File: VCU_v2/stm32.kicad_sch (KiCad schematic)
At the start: 1 part, among them J1 Conn_01x04

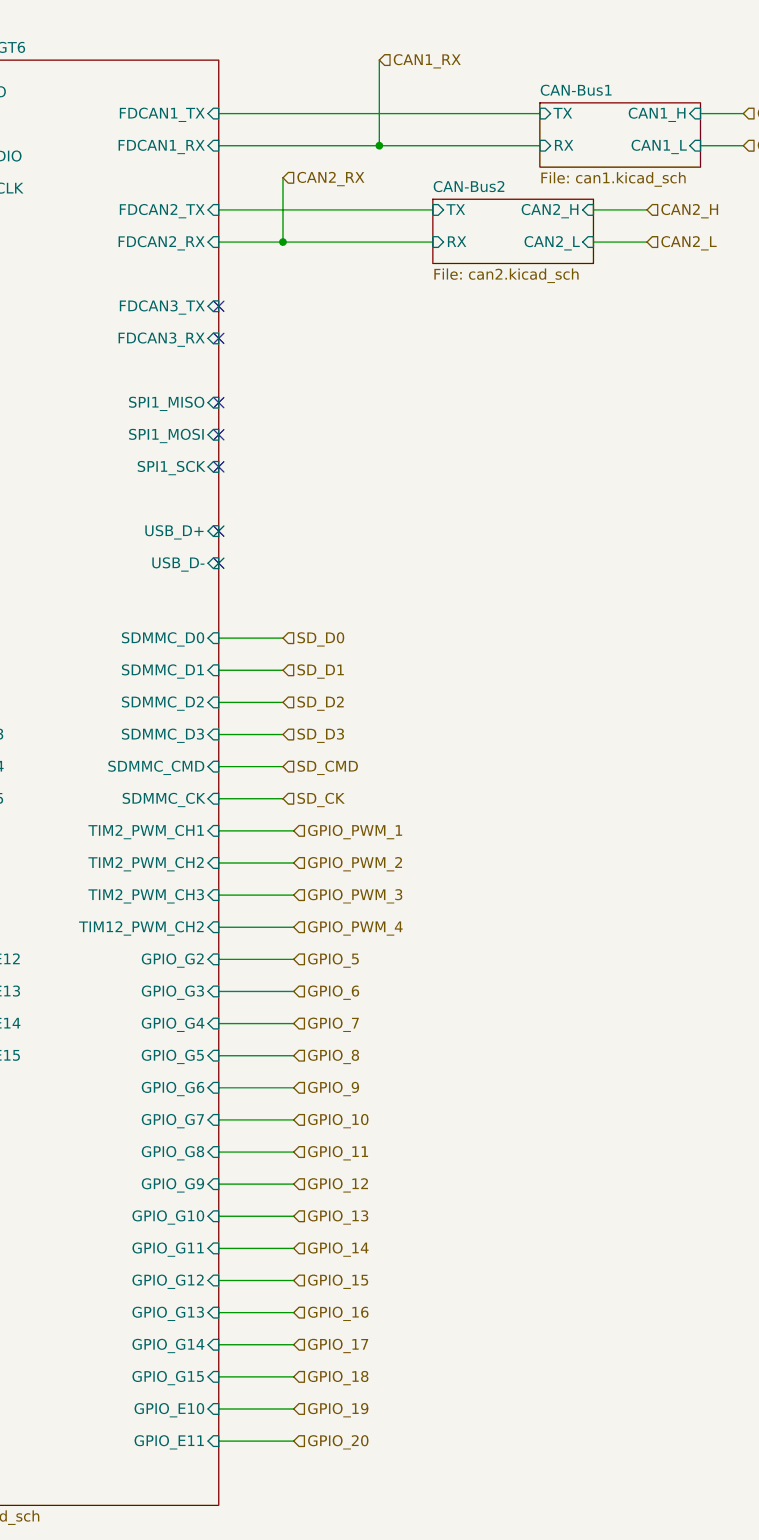
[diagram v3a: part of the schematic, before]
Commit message: slimed ethernet
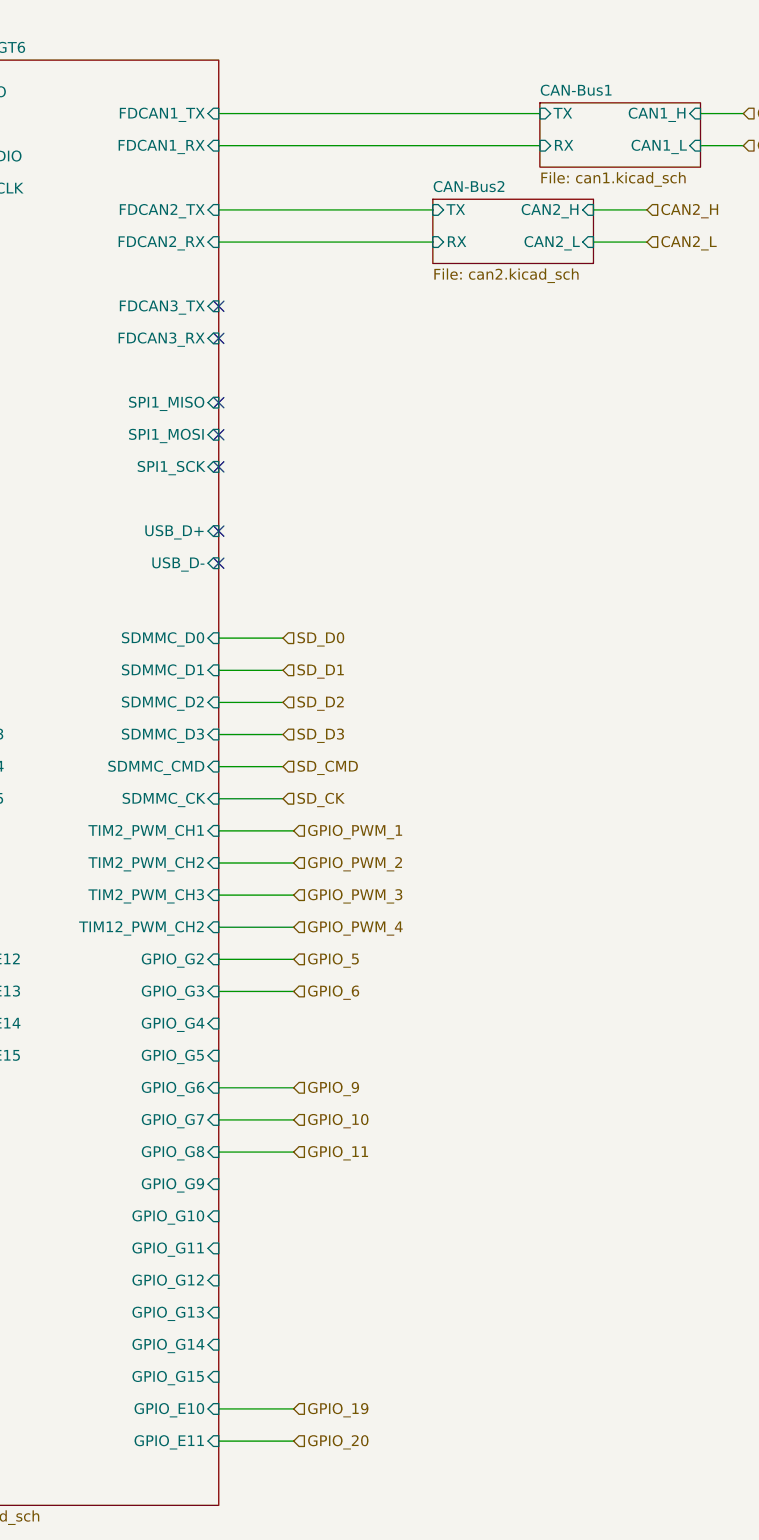
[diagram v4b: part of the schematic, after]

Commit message: Added connector for daq vcu
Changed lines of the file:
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@@
 	(wire
 		(pts
-			(xy 205.74 33.02) (xy 210.82 33.02)
+			(xy 205.74 33.02) (xy 226.06 33.02)
 		)
 		(stroke
@@
 	(wire
 		(pts
-			(xy 193.04 44.45) (xy 199.39 44.45)
+			(xy 193.04 44.45) (xy 226.06 44.45)
 		)
 		(stroke
@@
 	(wire
 		(pts
-			(xy 205.74 29.21) (xy 210.82 29.21)
+			(xy 205.74 29.21) (xy 226.06 29.21)
 		)
 		(stroke
@@
 	(wire
 		(pts
-			(xy 193.04 40.64) (xy 199.39 40.64)
+			(xy 193.04 40.64) (xy 226.06 40.64)
 		)
 		(stroke
@@
 	(hierarchical_label "CAN1_L"
 		(shape input)
-		(at 210.82 33.02 0)
+		(at 226.06 33.02 0)
 		(effects
 			(font
@@
 	(hierarchical_label "CAN2_L"
 		(shape input)
-		(at 199.39 44.45 0)
+		(at 226.06 44.45 0)
 		(effects
 			(font
@@
 	(hierarchical_label "CAN2_H"
 		(shape input)
-		(at 199.39 40.64 0)
+		(at 226.06 40.64 0)
 		(effects
 			(font
@@
 	(hierarchical_label "CAN1_H"
 		(shape input)
-		(at 210.82 29.21 0)
-		(effects
-			(font
+		(at 226.06 29.21 0)
+		(effects
+			(font
